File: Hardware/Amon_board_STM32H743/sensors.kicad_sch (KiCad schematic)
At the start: 32 parts, among them J10 GTFP08131Y2HR, J2 Conn_01x04_Pin, J3 Conn_01x04_Pin, J5 Conn_01x04_Pin, U6 MPU-6050, U7 BME280, U8 HMC5883L

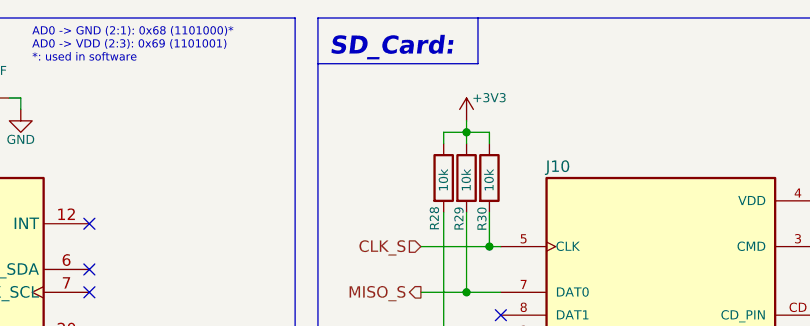
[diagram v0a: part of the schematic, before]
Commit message: Update: finished PCB v3, gerbers, ordered board, readme update
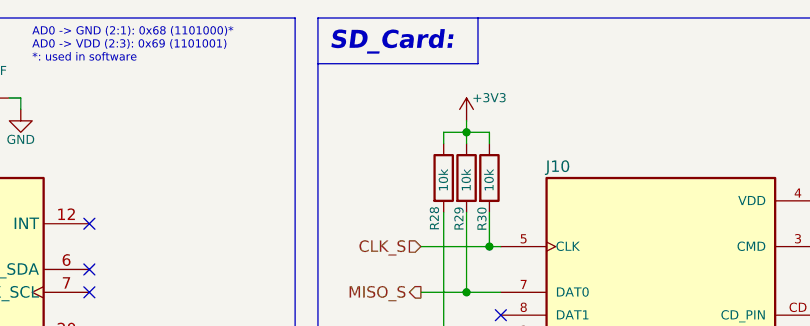
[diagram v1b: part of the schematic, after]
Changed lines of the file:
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@@
 				(bold yes)
 				(italic yes)
+				(color 132 0 0 1)
 			)
 			(justify left bottom)
@@
 				(bold yes)
 				(italic yes)
+				(color 132 0 0 1)
 			)
 			(justify left bottom)
@@
 				(bold yes)
 				(italic yes)
+				(color 132 0 0 1)
 			)
 			(justify left bottom)
@@
 				(bold yes)
 				(italic yes)
+				(color 132 0 0 1)
 			)
 			(justify left bottom)
@@
 				(bold yes)
 				(italic yes)
+				(color 132 0 0 1)
 			)
 			(justify left bottom)
@@
 				(bold yes)
 				(italic yes)
+				(color 132 0 0 1)
 			)
 			(justify left bottom)
@@
 				(bold yes)
 				(italic yes)
+				(color 132 0 0 1)
 			)
 			(justify left bottom)
@@
 	(text "SD_Card:"
 		(exclude_from_sim no)
-		(at 90.17 19.685 0)
+		(at 90.17 19.05 0)
 		(effects
 			(font
@@
 				(bold yes)
 				(italic yes)
+				(color 132 0 0 1)
 			)
 			(justify left bottom)
